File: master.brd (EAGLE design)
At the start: 56.1 x 93.9 mm, 70 parts, among them IC2 MCP1703-3302, M1 DHT22-NP, M2 NRF24L01P-M, Q1 IRLML2502, Q3 25MHz, SW1 EC11E_SW, U1 XMEGA-A3TQFP, U2 DS1302SOIC, U3 25LC640A-E/SN, U4 ENC28J60SO, X1 serial, X2 SPI/1W, X3 I2C, X4 ADC, X6 PS25_3W-R, X7 PS25_3W-R, X8 PS25_3W-R, X9 PS25_3W-R

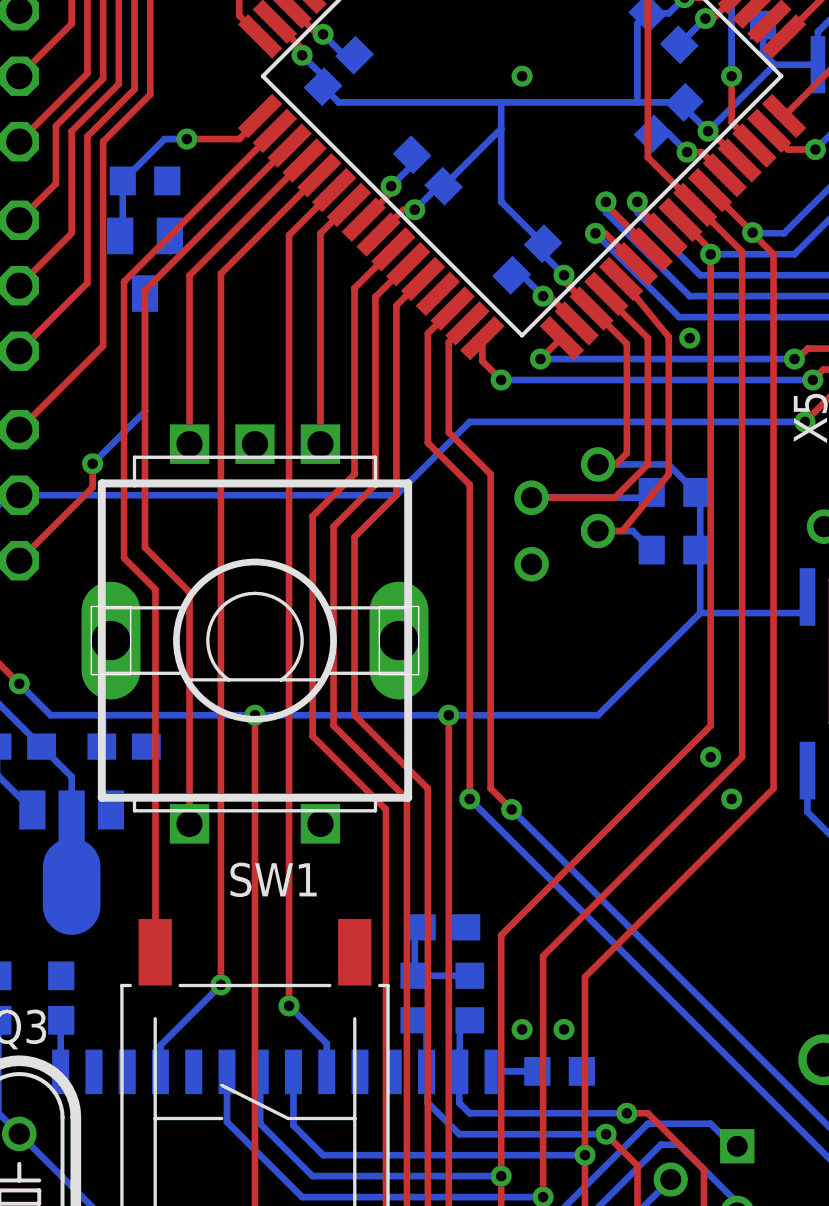
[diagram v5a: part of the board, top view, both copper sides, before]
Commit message: quadrature decoder needs two successive pins for input -> swapped s1
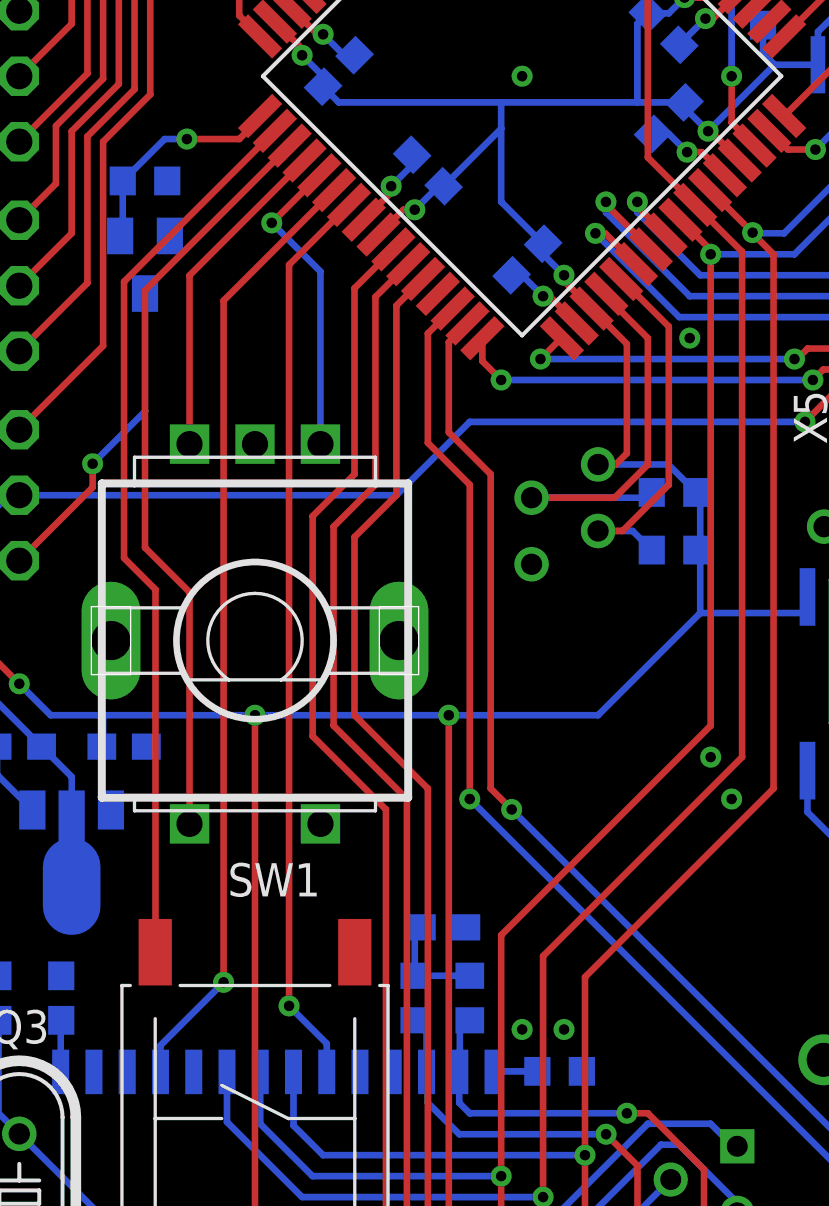
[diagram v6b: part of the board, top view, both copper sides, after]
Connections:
- net !LANCS: now also U1.23; no longer U1.22
- net !LANINT: now also U1.22; no longer U1.21
- net S1A: now also U1.21; no longer U1.23
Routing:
- net S1A: track 9.59 -> 11.8 mm, vias 0 -> 1
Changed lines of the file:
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@@
 <contactref element="X3" pad="3"/>
 <contactref element="U1" pad="37"/>
-<wire x1="38.98301875" y1="61.057178125" x2="40.8" y2="58.840196875" width="0.254" layer="1"/>
-<wire x1="40.8" y1="58.840196875" x2="40.8" y2="53.6" width="0.254" layer="1"/>
+<wire x1="40.8" y1="59.240196875" x2="40.8" y2="53.2" width="0.254" layer="1"/>
 <wire x1="38.1" y1="51.435" x2="39.035" y2="51.435" width="0.254" layer="1"/>
-<wire x1="39.035" y1="51.435" x2="40.8" y2="53.6" width="0.254" layer="1"/>
 <wire x1="38.1" y1="51.435" x2="39.42" y2="51.435" width="0.254" layer="16"/>
 <wire x1="39.42" y1="51.435" x2="40.15" y2="50.705" width="0.254" layer="16"/>
+<wire x1="40.8" y1="59.240196875" x2="38.98301875" y2="61.057178125" width="0.254" layer="1"/>
+<wire x1="39.035" y1="51.435" x2="40.8" y2="53.2" width="0.254" layer="1"/>
 </signal>
 <signal name="SS1WA">
@@
 <contactref element="U1" pad="20"/>
 <wire x1="22.5" y1="54.75" x2="22.5" y2="61.19116875" width="0.254" layer="1"/>
-<wire x1="22.5" y1="61.19116875" x2="26.89149375" y2="65.5826625" width="0.254" layer="1"/>
+<wire x1="26.89149375" y1="65.5826625" x2="22.5" y2="61.19116875" width="0.254" layer="1"/>
 </signal>
 <signal name="S1A">
 <contactref element="SW1" pad="A"/>
-<contactref element="U1" pad="23"/>
-<wire x1="27.5" y1="54.75" x2="27.5" y2="62.79705625" width="0.254" layer="1"/>
-<wire x1="27.5" y1="62.79705625" x2="28.58855" y2="63.88560625" width="0.254" layer="1"/>
+<contactref element="U1" pad="21"/>
+<wire x1="27.457178125" y1="65.016978125" x2="27.416978125" y2="65.016978125" width="0.254" layer="1"/>
+<wire x1="27.5" y1="62.1" x2="27.5" y2="61.3402" width="0" layer="19" extent="1-16"/>
+<wire x1="27.5" y1="61.3402" x2="27.5" y2="54.75" width="0.254" layer="16"/>
+<wire x1="27.457178125" y1="65.016978125" x2="25.6402" y2="63.2" width="0.254" layer="1"/>
+<via x="25.6402" y="63.2" extent="1-16" drill="0.4" shape="octagon"/>
+<wire x1="25.6402" y1="63.2" x2="27.5" y2="61.3402" width="0.254" layer="16"/>
 </signal>
 <signal name="S1P">
@@
 <signal name="!LANINT">
 <contactref element="U4" pad="4"/>
-<contactref element="U1" pad="21"/>
-<wire x1="27.457178125" y1="65.016978125" x2="23.7" y2="61.2598" width="0.254" layer="1"/>
-<wire x1="23.7" y1="61.2598" x2="23.7" y2="34.1" width="0.254" layer="1"/>
-<wire x1="23.7" y1="34.1" x2="21.39" y2="31.79" width="0.254" layer="16"/>
+<wire x1="23.8" y1="60.228425" x2="23.8" y2="34.2" width="0.254" layer="1"/>
+<wire x1="23.8" y1="34.2" x2="21.39" y2="31.79" width="0.254" layer="16"/>
 <wire x1="21.39" y1="31.79" x2="21.39" y2="30.78" width="0.254" layer="16"/>
-<via x="23.7" y="34.1" extent="1-16" drill="0.4" shape="octagon"/>
+<via x="23.8" y="34.2" extent="1-16" drill="0.4" shape="octagon"/>
+<contactref element="U1" pad="22"/>
+<wire x1="23.8" y1="60.228425" x2="28.022865625" y2="64.451290625" width="0.254" layer="1"/>
 </signal>
 <signal name="!LANCS">
 <contactref element="U4" pad="9"/>
-<contactref element="U1" pad="22"/>
-<wire x1="28.022865625" y1="64.451290625" x2="26.3" y2="62.728425" width="0.254" layer="1"/>
-<wire x1="26.3" y1="62.728425" x2="26.3" y2="33.3" width="0.254" layer="1"/>
+<wire x1="26.3" y1="61.59705625" x2="26.3" y2="33.3" width="0.254" layer="1"/>
 <wire x1="26.3" y1="33.3" x2="27.74" y2="31.86" width="0.254" layer="16"/>
 <via x="26.3" y="33.3" extent="1-16" drill="0.4" shape="octagon"/>
 <wire x1="27.74" y1="31.86" x2="27.74" y2="30.78" width="0.254" layer="16"/>
+<contactref element="U1" pad="23"/>
+<wire x1="26.3" y1="61.59705625" x2="28.58855" y2="63.88560625" width="0.254" layer="1"/>
 </signal>
 </signals>

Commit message: changed dru to mm, measured lan socket
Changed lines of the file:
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@@
 <layer number="23" name="tOrigins" color="15" fill="1" visible="yes" active="yes"/>
 <layer number="24" name="bOrigins" color="15" fill="1" visible="yes" active="yes"/>
-<layer number="25" name="tNames" color="7" fill="1" visible="yes" active="yes"/>
+<layer number="25" name="tNames" color="7" fill="1" visible="no" active="yes"/>
 <layer number="26" name="bNames" color="7" fill="1" visible="no" active="yes"/>
 <layer number="27" name="tValues" color="7" fill="1" visible="no" active="yes"/>
@@
 <layer number="38" name="bTest" color="7" fill="1" visible="no" active="yes"/>
 <layer number="39" name="tKeepout" color="4" fill="11" visible="yes" active="yes"/>
-<layer number="40" name="bKeepout" color="1" fill="11" visible="no" active="yes"/>
+<layer number="40" name="bKeepout" color="1" fill="11" visible="yes" active="yes"/>
 <layer number="41" name="tRestrict" color="4" fill="10" visible="yes" active="yes"/>
-<layer number="42" name="bRestrict" color="1" fill="10" visible="no" active="yes"/>
+<layer number="42" name="bRestrict" color="1" fill="10" visible="yes" active="yes"/>
 <layer number="43" name="vRestrict" color="2" fill="10" visible="yes" active="yes"/>
-<layer number="44" name="Drills" color="7" fill="1" visible="no" active="yes"/>
-<layer number="45" name="Holes" color="7" fill="1" visible="no" active="yes"/>
+<layer number="44" name="Drills" color="7" fill="1" visible="yes" active="yes"/>
+<layer number="45" name="Holes" color="7" fill="1" visible="yes" active="yes"/>
 <layer number="46" name="Milling" color="3" fill="1" visible="yes" active="yes"/>
-<layer number="47" name="Measures" color="7" fill="1" visible="no" active="yes"/>
-<layer number="48" name="Document" color="7" fill="1" visible="no" active="yes"/>
-<layer number="49" name="Reference" color="7" fill="1" visible="no" active="yes"/>
+<layer number="47" name="Measures" color="7" fill="1" visible="yes" active="yes"/>
+<layer number="48" name="Document" color="7" fill="1" visible="yes" active="yes"/>
+<layer number="49" name="Reference" color="7" fill="1" visible="yes" active="yes"/>
 <layer number="50" name="dxf" color="7" fill="1" visible="no" active="no"/>
 <layer number="51" name="tDocu" color="7" fill="1" visible="no" active="yes"/>
@@
 <layer number="98" name="Guide" color="6" fill="1" visible="no" active="no"/>
 <layer number="100" name="Muster" color="7" fill="1" visible="no" active="no"/>
-<layer number="101" name="Patch_Top" color="12" fill="4" visible="yes" active="yes"/>
-<layer number="102" name="Vscore" color="7" fill="1" visible="yes" active="yes"/>
-<layer number="104" name="Name" color="7" fill="1" visible="yes" active="yes"/>
-<layer number="116" name="Patch_BOT" color="9" fill="4" visible="yes" active="yes"/>
-<layer number="121" name="_tsilk" color="7" fill="1" visible="yes" active="yes"/>
-<layer number="122" name="_bsilk" color="7" fill="1" visible="yes" active="yes"/>
-<layer number="151" name="HeatSink" color="7" fill="1" visible="yes" active="yes"/>
 <layer number="153" name="FabDoc1" color="6" fill="1" visible="no" active="no"/>
 <layer number="154" name="FabDoc2" color="2" fill="1" visible="no" active="no"/>
@@
 <layer number="250" name="Descript" color="3" fill="1" visible="no" active="no"/>
 <layer number="251" name="SMDround" color="12" fill="11" visible="no" active="no"/>
-<layer number="254" name="cooling" color="7" fill="1" visible="yes" active="yes"/>
 </layers>
 <board>
@@
 <vertex x="50.5" y="39.25" curve="-90"/>
 </polygon>
+<dimension x1="47" y1="5.25" x2="56.85" y2="6" x3="51.925" y3="35.6" textsize="1.778" layer="47" dtype="horizontal"/>
+<dimension x1="47" y1="5.25" x2="61" y2="5.2" x3="54" y3="39.2" textsize="1.778" layer="47" dtype="horizontal"/>
 </plain>
 <attributes>
@@
 </class>
 </classes>
-<designrules name="bilex-cust *">
+<designrules name="bilex-cust">
 <description language="de">&lt;b&gt;Bilex Design Rules&lt;/b&gt;</description>
 <param name="layerSetup" value="(1*16)"/>
 <param name="mtCopper" value="0.035mm 0.035mm 0.035mm 0.035mm 0.035mm 0.035mm 0.035mm 0.035mm 0.035mm 0.035mm 0.035mm 0.035mm 0.035mm 0.035mm 0.035mm 0.035mm"/>
 <param name="mtIsolate" value="1.5mm 0.15mm 0.2mm 0.15mm 0.2mm 0.15mm 0.2mm 0.15mm 0.2mm 0.15mm 0.2mm 0.15mm 0.2mm 0.15mm 0.2mm"/>
-<param name="mdWireWire" value="10mil"/>
-<param name="mdWirePad" value="10mil"/>
-<param name="mdWireVia" value="10mil"/>
-<param name="mdPadPad" value="0.251459375mm"/>
-<param name="mdPadVia" value="10mil"/>
-<param name="mdViaVia" value="10mil"/>
-<param name="mdSmdPad" value="0.251459375mm"/>
-<param name="mdSmdVia" value="10mil"/>
-<param name="mdSmdSmd" value="0.251459375mm"/>
+<param name="mdWireWire" value="0.25mm"/>
+<param name="mdWirePad" value="0.25mm"/>
+<param name="mdWireVia" value="0.25mm"/>
+<param name="mdPadPad" value="0.25mm"/>
+<param name="mdPadVia" value="0.25mm"/>
+<param name="mdViaVia" value="0.25mm"/>
+<param name="mdSmdPad" value="0.25mm"/>
+<param name="mdSmdVia" value="0.25mm"/>
+<param name="mdSmdSmd" value="0.25mm"/>
 <param name="mdViaViaSameLayer" value="8mil"/>
 <param name="mnLayersViaInSmd" value="2"/>
@@
 <param name="mdDrill" value="8mil"/>
 <param name="mdSmdStop" value="0mil"/>
-<param name="msWidth" value="10mil"/>
+<param name="msWidth" value="0.25mm"/>
 <param name="msDrill" value="0.4mm"/>
 <param name="msMicroVia" value="9.99mm"/>
@@
 <wire x1="38" y1="14" x2="39.6" y2="14" width="0.254" layer="16"/>
 <wire x1="39.6" y1="14" x2="40.8" y2="12.8" width="0.254" layer="16"/>
-<wire x1="40.8" y1="12.8" x2="40.8" y2="5.87" width="0.254" layer="16"/>
+<wire x1="40.8" y1="12" x2="40.8" y2="5.87" width="0.254" layer="16"/>
 <wire x1="40.8" y1="5.87" x2="39.32" y2="4.39" width="0.254" layer="16"/>
-<wire x1="40.8" y1="12.8" x2="40.8" y2="12" width="0" layer="19" extent="16-16"/>
+<wire x1="40.8" y1="12.8" x2="40.8" y2="12" width="0.254" layer="16"/>
 </signal>
 <signal name="MOSI">
@@
 <contactref element="U1" pad="21"/>
 <wire x1="27.457178125" y1="65.016978125" x2="27.416978125" y2="65.016978125" width="0.254" layer="1"/>
-<wire x1="27.5" y1="62.1" x2="27.5" y2="61.3402" width="0" layer="19" extent="1-16"/>
 <wire x1="27.5" y1="61.3402" x2="27.5" y2="54.75" width="0.254" layer="16"/>
 <wire x1="27.457178125" y1="65.016978125" x2="25.6402" y2="63.2" width="0.254" layer="1"/>
